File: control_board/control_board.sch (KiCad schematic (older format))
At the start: 38 parts, among them J1 Conn_01x08_Male, K1 G5Q-1A, Q1 Q_NPN_BEC, U1 MC78M05_TO252, U2 TSR_1-24120, U3 74LS02, U4 74LS02, U5 Conn_01x08_Male

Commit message: Draft logic layout
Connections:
- net +12V: now also RN3.7 (R7.1), RN3.8 (R8.1); no longer RN3.4 (R4.1), RN3.5 (R5.1)
- net +5V: now also RN1.7 (R7.1), RN2.14 (R3.2), RN3.16 (R1.2); no longer RN1.6 (R6.1), RN2.10 (R7.2), RN2.13 (R4.2), RN3.8 (R8.1)
- net GND: now also RN1.16 (R1.2), RN2.10 (R7.2), RN2.13 (R4.2), RN2.2 (R2.1); no longer RN1.2 (R2.1), RN2.14 (R3.2), RN2.15 (R2.2), RN2.16 (R1.2)
- net aref_1k1: now also A1.8 (D5), RN1.15 (R2.2); no longer A1.10 (D7), RN1.4 (R4.1)
- net aref_1k2: now also A1.9 (D6), RN1.14 (R3.2); no longer A1.11 (D8)
- net aref_330: now also RN3.15 (R2.2); no longer RN3.7 (R7.1)
- net p_cmd: now also RN2.1 (R1.1), U3.13; no longer RN1.1 (R1.1), U3.10
- net p_rqst: now also RN1.1 (R1.1); no longer RN2.1 (R1.1)
- net pot_a: now also RN3.1 (R1.1); no longer RN3.9 (R8.2)
- net sensor_a: now also RN1.8 (R8.1); no longer RN1.9 (R8.2)
- net sr_rst: now also RN2.5 (R5.1), U3.8; no longer RN2.2 (R2.1), U3.3
- net th1_tap: now also A1.10 (D7), RN1.12 (R5.2); no longer A1.8 (D5), RN1.10 (R7.2)
- net th2_tap: now also A1.11 (D8), RN1.10 (R7.2), RN1.9 (R8.2); no longer A1.9 (D6), RN1.12 (R5.2), RN1.8 (R8.1)
- net wd_kick: now also RN2.7 (R7.1); no longer RN2.3 (R3.1)
- net at A1.21 (A2), C10.1, TH1.1: now also RN1.6 (R6.1); no longer RN1.7 (R7.1)
- net at D4.2 (A): now also RN3.5 (R5.1); no longer RN3.16 (R1.2)
- net at U4.1, U4.5: now also RN2.3 (R3.1), U3.9; no longer RN2.4 (R4.1), U3.2
- net at U4.3, U4.4: now also RN2.4 (R4.1); no longer RN2.5 (R5.1)
- net at D5.2 (A), RN3.14 (R3.2): now also RN3.13 (R4.2); no longer RN3.15 (R2.2)
- net at U3.4: now also U3.11; no longer U3.9
- net at D6.2 (A): now also RN3.6 (R6.1); no longer RN3.11 (R6.2)
- net at RN3.12 (R5.2): now also RN3.9 (R8.2); no longer RN3.6 (R6.1)
- net raref_1k2: no longer names the net of RN1.3 (R3.1)
- net raref_1k2: now also A1.18 (AREF), C7.1, RN1.2 (R2.1), RN3.2 (R2.1)
- new net: Q1.1 (B), RN2.15 (R2.2), RN2.16 (R1.2)
- new net: U3.1, U3.12
- new net: RN3.3 (R3.1), RN3.4 (R4.1), U3.10, U3.2, U3.3
- new net: RN3.10 (R7.2), RN3.11 (R6.2)
- now unconnected: RN1.13 (R4.2)
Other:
- moved on the sheet: RN1A, RN1B, RN1C, RN1D, RN1E, RN1F, RN1G, RN2A, RN2B, RN2C, RN2D, RN2E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

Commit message: Layout almost done
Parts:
- added C13, C14: 2.2u, Capacitor_SMD:C_0805_2012Metric_Pad1.18x1.45mm_HandSolder, symbol Device:C
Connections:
- net +12V: now also C13.1
- net +5V: now also D2.3 (K), RN1.4 (R4.1), C14.1; no longer D2.1 (K)
- net GND: now also C13.2, C14.2
- net pot_a: now also D2.1 (K); no longer D2.5 (K)
- net sensor_a: now also D2.5 (K); no longer D2.3 (K)
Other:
- moved on the sheet: RN1D, U1
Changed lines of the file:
@@
 L Regulator_Linear:MC78M05_TO252 U1
 U 1 1 6001E56B
-P 5900 1850
-F 0 "U1" H 5900 2092 50  0000 C CNN
-F 1 "MC78M05_TO252" H 5900 2001 50  0000 C CNN
-F 2 "Package_TO_SOT_SMD:TO-252-2" H 5900 2075 50  0001 C CIN
-F 3 "https://www.onsemi.com/pub/Collateral/MC78M00-D.PDF" H 5900 1800 50  0001 C CNN
-	1    5900 1850
+P 6150 1850
+F 0 "U1" H 6150 2092 50  0000 C CNN
+F 1 "MC78M05_TO252" H 6150 2001 50  0000 C CNN
+F 2 "Package_TO_SOT_SMD:TO-252-2" H 6150 2075 50  0001 C CIN
+F 3 "https://www.onsemi.com/pub/Collateral/MC78M00-D.PDF" H 6150 1800 50  0001 C CNN
+	1    6150 1850
 	1    0    0    -1
 $EndComp
@@
 Wire Wire Line
 	5150 1850 5350 1850
-Wire Wire Line
-	5350 1850 5600 1850
 Connection ~ 5350 1850
 $Comp
@@
 	4650 1850 4850 1850
 Connection ~ 4250 2150
-Wire Wire Line
-	5900 2150 6950 2150
-Connection ~ 5900 2150
 $Comp
 L power:+12V #PWR03
@@
 	4850 2150 5350 2150
 Wire Wire Line
-	5350 2150 5900 2150
+	5350 2150 5700 2150
 Connection ~ 5350 2150
 $Comp
@@
 L power:+5V #PWR09
 U 1 1 600C4C55
-P 5650 3350
-F 0 "#PWR09" H 5650 3200 50  0001 C CNN
-F 1 "+5V" H 5665 3523 50  0000 C CNN
-F 2 "" H 5650 3350 50  0001 C CNN
-F 3 "" H 5650 3350 50  0001 C CNN
-	1    5650 3350
-	1    0    0    -1
-$EndComp
-Text Label 6000 3350 1    50   ~ 0
+P 5750 3350
+F 0 "#PWR09" H 5750 3200 50  0001 C CNN
+F 1 "+5V" H 5765 3523 50  0000 C CNN
+F 2 "" H 5750 3350 50  0001 C CNN
+F 3 "" H 5750 3350 50  0001 C CNN
+	1    5750 3350
+	1    0    0    -1
+$EndComp
+Text Label 6050 3350 1    50   ~ 0
 pot_a
-Text Label 5800 3350 1    50   ~ 0
+Text Label 5950 3350 1    50   ~ 0
 sensor_a
 Connection ~ 6200 5550
@@
 	0    -1   -1   0
 $EndComp
-Wire Wire Line
-	6050 3350 5950 3350
-Wire Wire Line
-	5850 3350 5750 3350
 $Comp
 L Device:R_Pack08_Split RN3
@@
 L Device:R_Pack08_Split RN1
 U 4 1 60CA5856
-P 3850 6550
-F 0 "RN1" V 3750 6450 50  0000 L CNN
-F 1 "R_Pack08_Split" H 3938 6505 50  0001 L CNN
-F 2 "Package_SO:SOIC-16_4.55x10.3mm_P1.27mm" V 3770 6550 50  0001 C CNN
-F 3 "~" H 3850 6550 50  0001 C CNN
-	4    3850 6550
-	-1   0    0    1
+P 7600 4500
+F 0 "RN1" V 7500 4400 50  0000 L CNN
+F 1 "R_Pack08_Split" H 7688 4455 50  0001 L CNN
+F 2 "Package_SO:SOIC-16_4.55x10.3mm_P1.27mm" V 7520 4500 50  0001 C CNN
+F 3 "~" H 7600 4500 50  0001 C CNN
+	4    7600 4500
+	1    0    0    -1
 $EndComp
 $Comp
@@
 Text Label 5450 1850 0    50   ~ 0
 hc_02
-Text Label 6250 1850 0    50   ~ 0
+Text Label 6700 1850 0    50   ~ 0
 hc_03
 Text Label 2750 4650 0    50   ~ 0
@@
 	1    0    0    -1
 $EndComp
-Wire Wire Line
-	6200 1850 6950 1850
 Text Label 1000 7050 2    50   ~ 0
 th1_tap
@@
 Text Label 2650 6150 1    50   ~ 0
 aref_1k2
+$Comp
+L Device:C C13
+U 1 1 60BEF2F8
+P 5700 2000
+F 0 "C13" H 5550 2100 50  0000 L CNN
+F 1 "2.2u" H 5550 1900 50  0000 L CNN
+F 2 "Capacitor_SMD:C_0805_2012Metric_Pad1.18x1.45mm_HandSolder" H 5738 1850 50  0001 C CNN
+F 3 "~" H 5700 2000 50  0001 C CNN
+	1    5700 2000
+	1    0    0    -1
+$EndComp
+Connection ~ 5700 2150
+$Comp
+L Device:C C14
+U 1 1 60BFDBB0
+P 6700 2000
+F 0 "C14" H 6550 2100 50  0000 L CNN
+F 1 "2.2u" H 6550 1900 50  0000 L CNN
+F 2 "Capacitor_SMD:C_0805_2012Metric_Pad1.18x1.45mm_HandSolder" H 6738 1850 50  0001 C CNN
+F 3 "~" H 6700 2000 50  0001 C CNN
+	1    6700 2000
+	1    0    0    -1
+$EndComp
+Wire Wire Line
+	6700 1850 6950 1850
+Connection ~ 6700 2150
+Wire Wire Line
+	6700 2150 6950 2150
+Wire Wire Line
+	5700 2150 6150 2150
+Connection ~ 6150 2150
+Wire Wire Line
+	6150 2150 6700 2150
+Wire Wire Line
+	6700 1850 6450 1850
+Connection ~ 6700 1850
+Wire Wire Line
+	5850 1850 5700 1850
+Wire Wire Line
+	5350 1850 5700 1850
+Connection ~ 5700 1850
+Text Label 5650 3350 1    50   ~ 0
+pot_a
+Text Label 5850 3350 1    50   ~ 0
+sensor_a
 $EndSCHEMATC

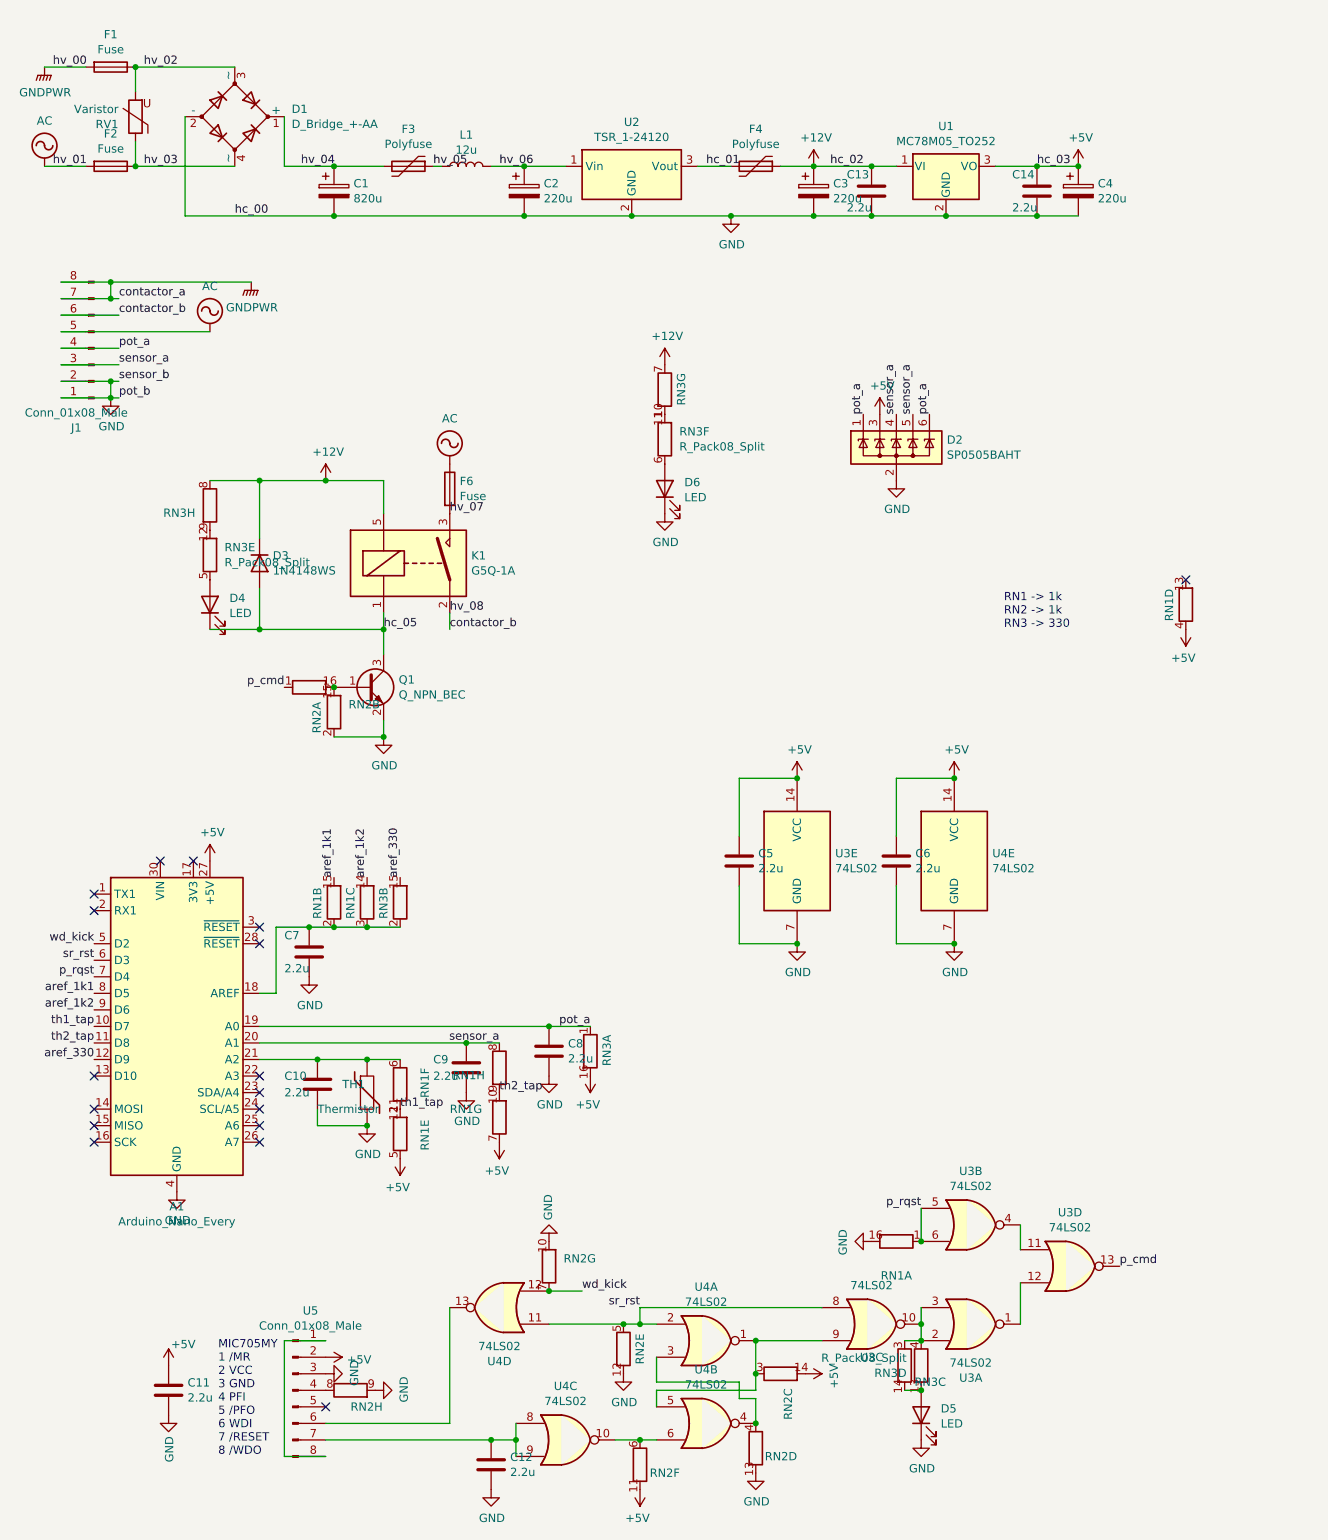
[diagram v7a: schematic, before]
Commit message: Layout complete
TODO
Via stitch ground
Fix silkscreen positions
Final check of revision notes
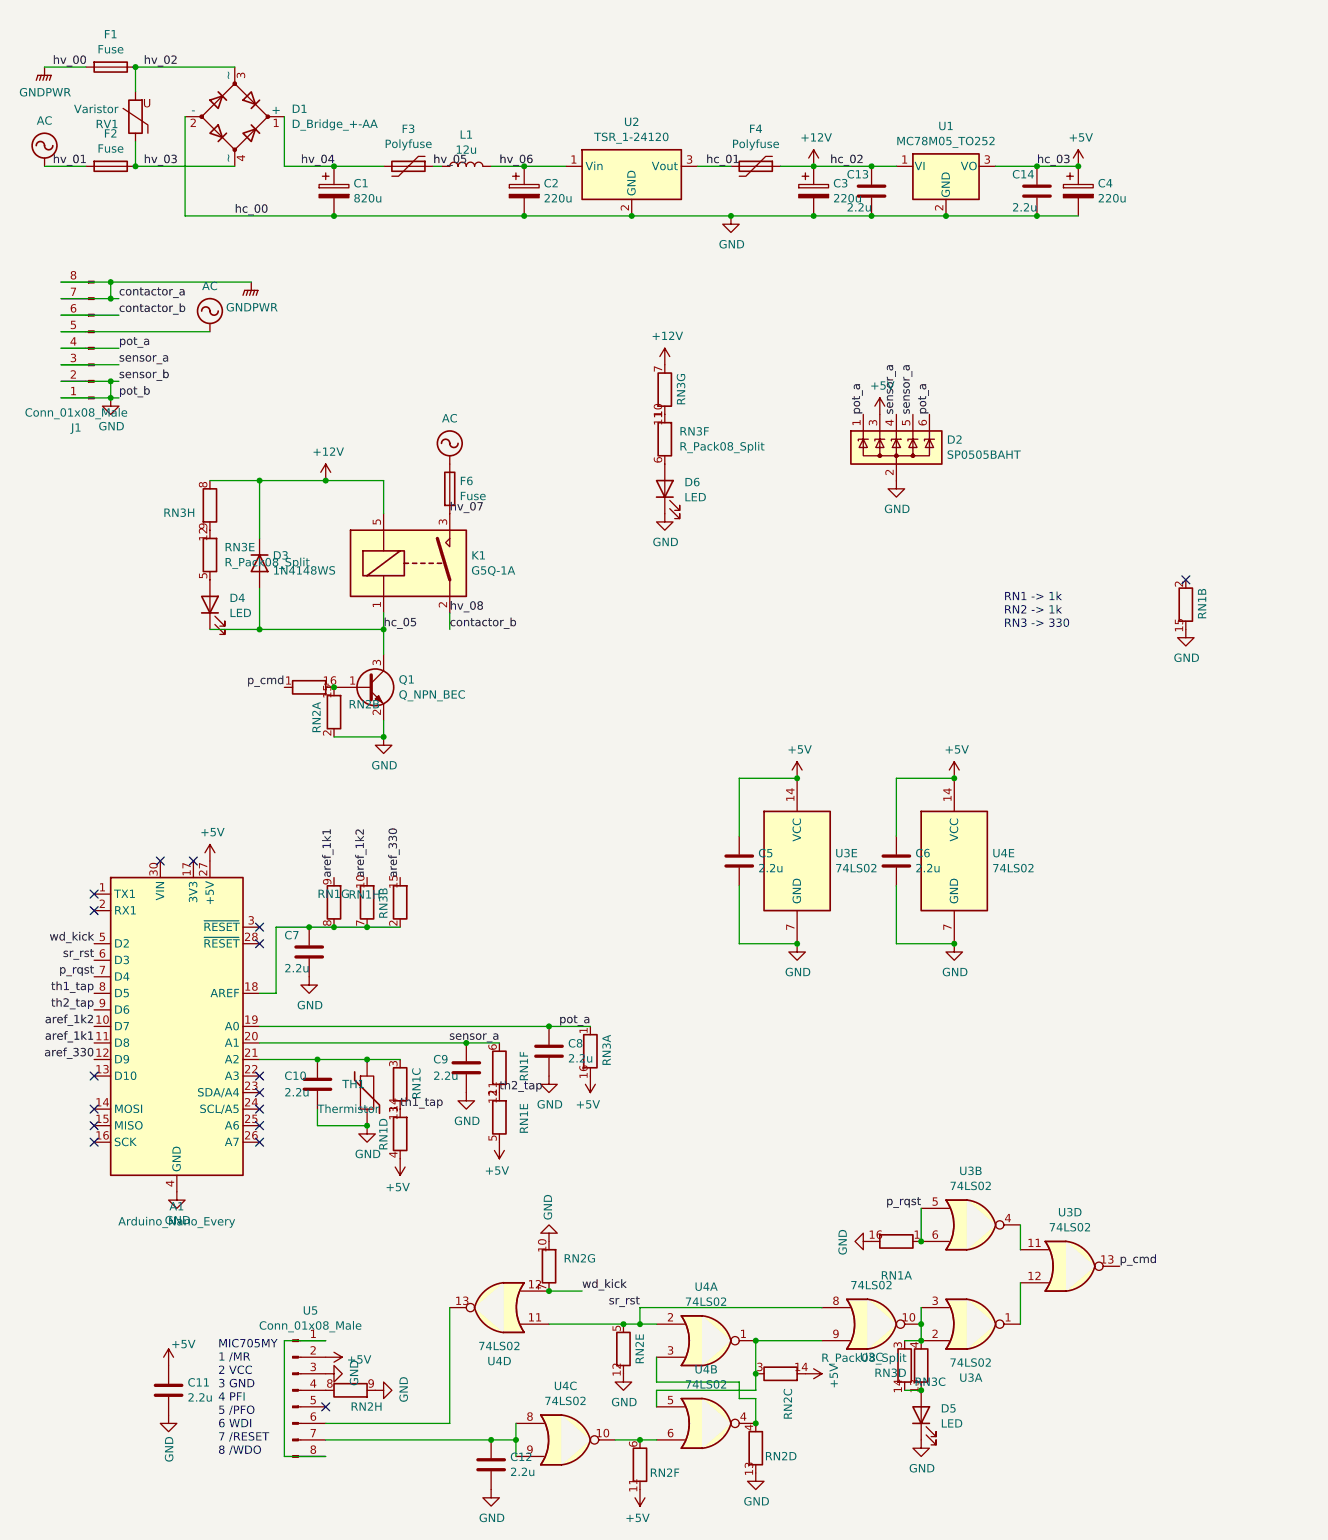
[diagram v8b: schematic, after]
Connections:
- net +5V: no longer RN1.7 (R7.1)
- net GND: now also RN1.15 (R2.2)
- net aref_1k1: now also A1.11 (D8), RN1.9 (R8.2); no longer A1.8 (D5), RN1.15 (R2.2)
- net aref_1k2: now also A1.10 (D7), RN1.10 (R7.2); no longer A1.9 (D6), RN1.14 (R3.2)
- net sensor_a: now also RN1.6 (R6.1); no longer RN1.8 (R8.1)
- net th1_tap: now also A1.8 (D5), RN1.13 (R4.2), RN1.14 (R3.2); no longer A1.10 (D7), RN1.11 (R6.2), RN1.12 (R5.2)
- net th2_tap: now also A1.9 (D6), RN1.11 (R6.2), RN1.12 (R5.2); no longer A1.11 (D8), RN1.10 (R7.2), RN1.9 (R8.2)
- net at A1.18 (AREF), C7.1, RN3.2 (R2.1): now also RN1.7 (R7.1), RN1.8 (R8.1); no longer RN1.2 (R2.1), RN1.3 (R3.1)
- net at A1.21 (A2), C10.1, TH1.1: now also RN1.3 (R3.1); no longer RN1.6 (R6.1)
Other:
- moved on the sheet: RN1B, RN1C, RN1D, RN1E, RN1F, RN1G, RN1H
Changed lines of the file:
@@
 L Device:R_Pack08_Split RN1
 U 2 1 60C44838
-P 2450 6300
-F 0 "RN1" V 2350 6200 50  0000 L CNN
-F 1 "R_Pack08_Split" H 2538 6255 50  0001 L CNN
-F 2 "Package_SO:SOIC-16_4.55x10.3mm_P1.27mm" V 2370 6300 50  0001 C CNN
-F 3 "~" H 2450 6300 50  0001 C CNN
-	2    2450 6300
-	1    0    0    -1
+P 7600 4500
+F 0 "RN1" V 7500 4400 50  0000 L CNN
+F 1 "R_Pack08_Split" H 7688 4455 50  0001 L CNN
+F 2 "Package_SO:SOIC-16_4.55x10.3mm_P1.27mm" V 7520 4500 50  0001 C CNN
+F 3 "~" H 7600 4500 50  0001 C CNN
+	2    7600 4500
+	-1   0    0    1
 $EndComp
 $Comp
@@
 $Comp
 L Device:R_Pack08_Split RN1
-U 3 1 60CA6899
-P 2650 6300
-F 0 "RN1" V 2550 6200 50  0000 L CNN
-F 1 "R_Pack08_Split" H 2738 6255 50  0001 L CNN
-F 2 "Package_SO:SOIC-16_4.55x10.3mm_P1.27mm" V 2570 6300 50  0001 C CNN
-F 3 "~" H 2650 6300 50  0001 C CNN
-	3    2650 6300
-	1    0    0    -1
-$EndComp
-$Comp
-L Device:R_Pack08_Split RN1
-U 8 1 60CA7819
+U 6 1 60CA8167
 P 3450 7300
-F 0 "RN1" H 3538 7346 50  0000 L CNN
+F 0 "RN1" V 3300 7200 50  0000 L CNN
 F 1 "R_Pack08_Split" H 3538 7255 50  0001 L CNN
 F 2 "Package_SO:SOIC-16_4.55x10.3mm_P1.27mm" V 3370 7300 50  0001 C CNN
 F 3 "~" H 3450 7300 50  0001 C CNN
-	8    3450 7300
-	-1   0    0    1
-$EndComp
-$Comp
-L Device:R_Pack08_Split RN1
-U 6 1 60CA8167
-P 2850 7400
-F 0 "RN1" V 2700 7300 50  0000 L CNN
-F 1 "R_Pack08_Split" H 2938 7355 50  0001 L CNN
-F 2 "Package_SO:SOIC-16_4.55x10.3mm_P1.27mm" V 2770 7400 50  0001 C CNN
-F 3 "~" H 2850 7400 50  0001 C CNN
-	6    2850 7400
+	6    3450 7300
 	-1   0    0    1
 $EndComp
@@
 L Device:R_Pack08_Split RN1
 U 5 1 60CAA263
-P 2850 7700
-F 0 "RN1" V 3000 7600 50  0000 L CNN
-F 1 "R_Pack08_Split" H 2938 7655 50  0001 L CNN
-F 2 "Package_SO:SOIC-16_4.55x10.3mm_P1.27mm" V 2770 7700 50  0001 C CNN
-F 3 "~" H 2850 7700 50  0001 C CNN
-	5    2850 7700
+P 3450 7600
+F 0 "RN1" V 3600 7500 50  0000 L CNN
+F 1 "R_Pack08_Split" H 3538 7555 50  0001 L CNN
+F 2 "Package_SO:SOIC-16_4.55x10.3mm_P1.27mm" V 3370 7600 50  0001 C CNN
+F 3 "~" H 3450 7600 50  0001 C CNN
+	5    3450 7600
 	1    0    0    -1
 $EndComp
@@
 $Comp
 L Device:R_Pack08_Split RN3
-U 2 1 612C76DA
-P 2850 6300
-F 0 "RN3" V 2750 6200 50  0000 L CNN
-F 1 "R_Pack08_Split" H 2900 6700 50  0001 L CNN
-F 2 "Package_SO:SOIC-16_4.55x10.3mm_P1.27mm" V 2770 6300 50  0001 C CNN
-F 3 "~" H 2850 6300 50  0001 C CNN
-	2    2850 6300
-	1    0    0    -1
-$EndComp
-$Comp
-L Device:R_Pack08_Split RN3
 U 5 1 612C8EC0
 P 1700 4200
@@
 L Device:R_Pack08_Split RN1
 U 4 1 60CA5856
-P 7600 4500
-F 0 "RN1" V 7500 4400 50  0000 L CNN
-F 1 "R_Pack08_Split" H 7688 4455 50  0001 L CNN
-F 2 "Package_SO:SOIC-16_4.55x10.3mm_P1.27mm" V 7520 4500 50  0001 C CNN
-F 3 "~" H 7600 4500 50  0001 C CNN
-	4    7600 4500
-	1    0    0    -1
-$EndComp
-$Comp
-L power:+5V #PWR0102
-U 1 1 609738AF
-P 7600 4650
-F 0 "#PWR0102" H 7600 4500 50  0001 C CNN
-F 1 "+5V" H 7615 4823 50  0000 C CNN
-F 2 "" H 7600 4650 50  0001 C CNN
-F 3 "" H 7600 4650 50  0001 C CNN
-	1    7600 4650
-	-1   0    0    1
+P 2850 7700
+F 0 "RN1" V 2750 7600 50  0000 L CNN
+F 1 "R_Pack08_Split" H 2938 7655 50  0001 L CNN
+F 2 "Package_SO:SOIC-16_4.55x10.3mm_P1.27mm" V 2770 7700 50  0001 C CNN
+F 3 "~" H 2850 7700 50  0001 C CNN
+	4    2850 7700
+	1    0    0    -1
 $EndComp
 Text Label 750  1250 0    50   ~ 0
@@
 $EndComp
 Connection ~ 6000 9250
-$Comp
-L Device:R_Pack08_Split RN1
-U 7 1 60CA927C
-P 3450 7600
-F 0 "RN1" H 3150 7650 50  0000 L CNN
-F 1 "R_Pack08_Split" H 3538 7555 50  0001 L CNN
-F 2 "Package_SO:SOIC-16_4.55x10.3mm_P1.27mm" V 3370 7600 50  0001 C CNN
-F 3 "~" H 3450 7600 50  0001 C CNN
-	7    3450 7600
-	1    0    0    -1
-$EndComp
 Connection ~ 2450 5000
 Wire Wire Line
@@
 	1    0    0    -1
 $EndComp
-Text Label 1000 7050 2    50   ~ 0
+Text Label 1000 6850 2    50   ~ 0
 th1_tap
-Text Label 1000 7150 2    50   ~ 0
+Text Label 1000 6950 2    50   ~ 0
 th2_tap
 Text Label 3450 7450 0    50   ~ 0
@@
 Text Label 1000 7250 2    50   ~ 0
 aref_330
-Text Label 1000 6950 2    50   ~ 0
+Text Label 1000 7050 2    50   ~ 0
 aref_1k2
-Text Label 1000 6850 2    50   ~ 0
+Text Label 1000 7150 2    50   ~ 0
 aref_1k1
 $Comp
@@
 	2300 6450 2450 6450
 Connection ~ 2450 6450
-Wire Wire Line
-	2450 6450 2650 6450
-Connection ~ 2650 6450
-Wire Wire Line
-	2650 6450 2850 6450
 Text Label 2650 6150 1    50   ~ 0
 aref_1k2
@@
 Text Label 5850 3350 1    50   ~ 0
 sensor_a
+$Comp
+L Device:R_Pack08_Split RN1
+U 7 1 60CA927C
+P 2650 6300
+F 0 "RN1" H 2350 6350 50  0000 L CNN
+F 1 "R_Pack08_Split" H 2738 6255 50  0001 L CNN
+F 2 "Package_SO:SOIC-16_4.55x10.3mm_P1.27mm" V 2570 6300 50  0001 C CNN
+F 3 "~" H 2650 6300 50  0001 C CNN
+	7    2650 6300
+	1    0    0    -1
+$EndComp
+$Comp
+L Device:R_Pack08_Split RN1
+U 8 1 60CA7819
+P 2450 6300
+F 0 "RN1" H 2538 6346 50  0000 L CNN
+F 1 "R_Pack08_Split" H 2538 6255 50  0001 L CNN
+F 2 "Package_SO:SOIC-16_4.55x10.3mm_P1.27mm" V 2370 6300 50  0001 C CNN
+F 3 "~" H 2450 6300 50  0001 C CNN
+	8    2450 6300
+	1    0    0    -1
+$EndComp
+$Comp
+L Device:R_Pack08_Split RN1
+U 3 1 60CA6899
+P 2850 7400
+F 0 "RN1" V 2750 7300 50  0000 L CNN
+F 1 "R_Pack08_Split" H 2938 7355 50  0001 L CNN
+F 2 "Package_SO:SOIC-16_4.55x10.3mm_P1.27mm" V 2770 7400 50  0001 C CNN
+F 3 "~" H 2850 7400 50  0001 C CNN
+	3    2850 7400
+	-1   0    0    1
+$EndComp
+$Comp
+L Device:R_Pack08_Split RN3
+U 2 1 612C76DA
+P 2850 6300
+F 0 "RN3" V 2750 6200 50  0000 L CNN
+F 1 "R_Pack08_Split" H 2900 6700 50  0001 L CNN
+F 2 "Package_SO:SOIC-16_4.55x10.3mm_P1.27mm" V 2770 6300 50  0001 C CNN
+F 3 "~" H 2850 6300 50  0001 C CNN
+	2    2850 6300
+	1    0    0    -1
+$EndComp
+Wire Wire Line
+	2450 6450 2650 6450
+Connection ~ 2650 6450
+Wire Wire Line
+	2650 6450 2850 6450
+$Comp
+L power:GND #PWR0102
+U 1 1 60D3AD85
+P 7600 4650
+F 0 "#PWR0102" H 7600 4400 50  0001 C CNN
+F 1 "GND" H 7605 4477 50  0000 C CNN
+F 2 "" H 7600 4650 50  0001 C CNN
+F 3 "" H 7600 4650 50  0001 C CNN
+	1    7600 4650
+	1    0    0    -1
+$EndComp
 $EndSCHEMATC
